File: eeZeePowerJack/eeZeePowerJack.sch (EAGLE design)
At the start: 10 parts, among them J1 POWER_JACKPTH, U2 LD29150DT

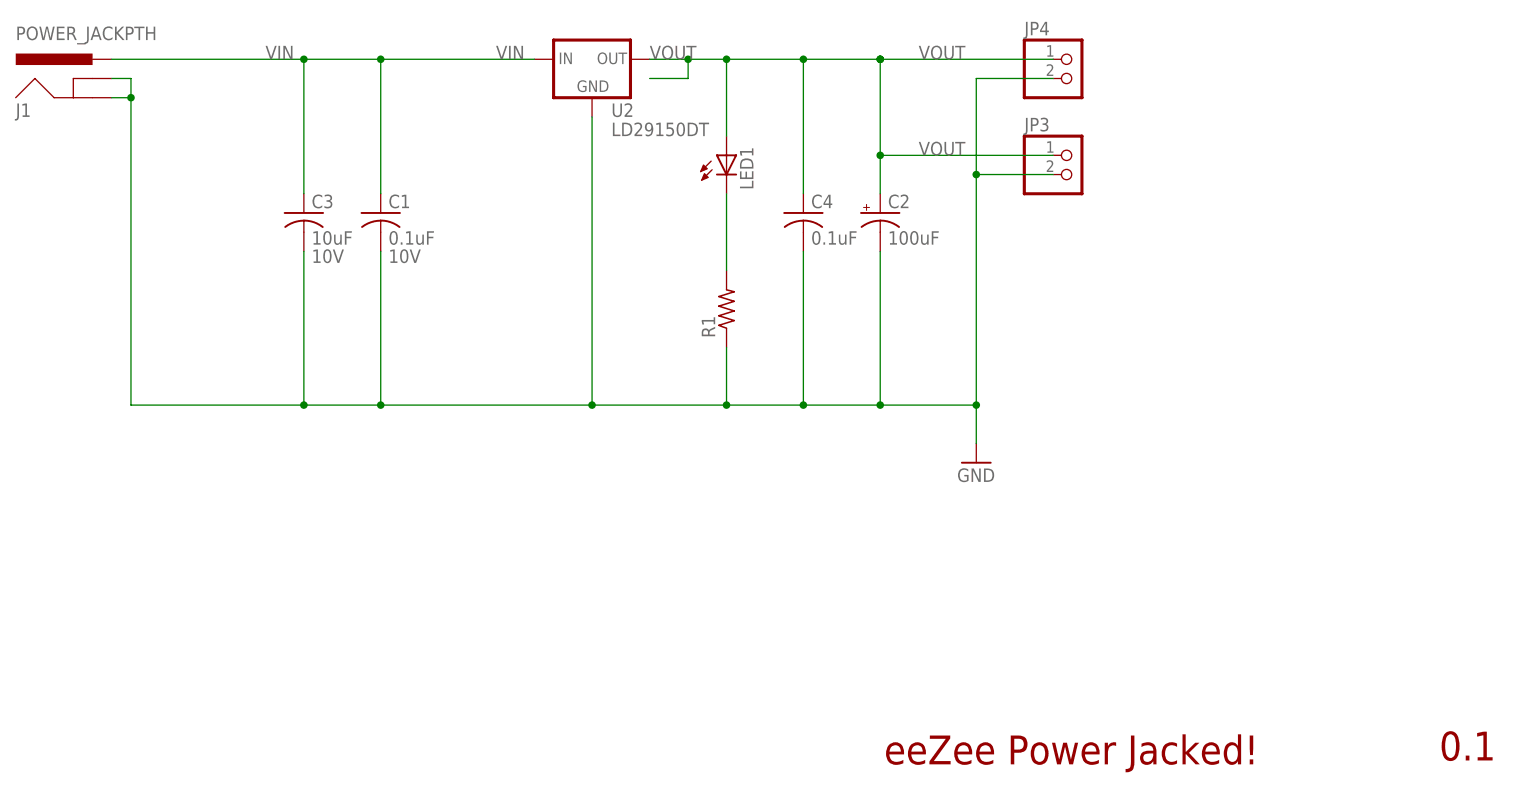
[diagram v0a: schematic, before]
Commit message: Revised to use standard 1206 10uF part, moved bot thoughts silk.
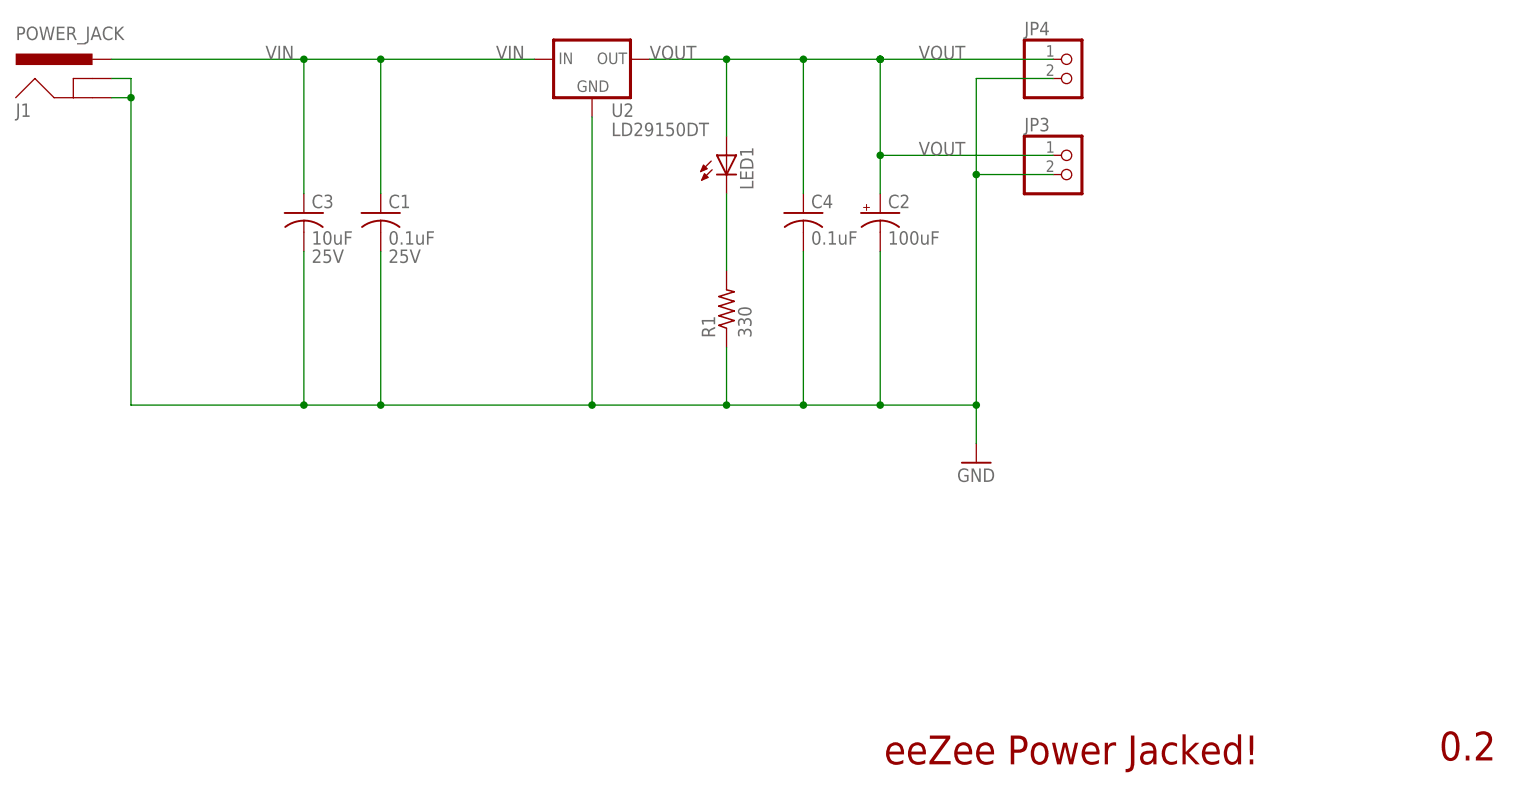
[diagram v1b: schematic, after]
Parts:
- C1: VOLTAGE 10V -> 25V
- C3: device rcl:C-USC0603 -> rcl:C-USC1206; VOLTAGE 10V -> 25V
- J1: value POWER_JACKPTH -> POWER_JACK
- R1: value (none) -> 330
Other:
- note added: "0.2"
- note removed: "0.1"
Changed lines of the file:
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@@
 <part name="LED1" library="led" deviceset="LED" device="CHIPLED_1206"/>
 <part name="C1" library="rcl" deviceset="C-US" device="C0603" value="0.1uF">
-<attribute name="VOLTAGE" value="10V"/>
+<attribute name="VOLTAGE" value="25V"/>
 </part>
 <part name="C2" library="rcl" deviceset="CPOL-US" device="SMCB" value="100uF"/>
-<part name="R1" library="resistor" deviceset="R-US_" device="R0603"/>
-<part name="C3" library="rcl" deviceset="C-US" device="C0603" value="10uF">
-<attribute name="VOLTAGE" value="10V"/>
+<part name="R1" library="resistor" deviceset="R-US_" device="R0603" value="330"/>
+<part name="C3" library="rcl" deviceset="C-US" device="C1206" value="10uF">
+<attribute name="VOLTAGE" value="25V"/>
 </part>
 <part name="FRAME1" library="mes" deviceset="LETTER_L" device=""/>
@@
 <part name="JP3" library="pinhead-2" deviceset="PINHD-1X02" device="_2.54-S"/>
 <part name="JP4" library="pinhead-2" deviceset="PINHD-1X02" device="_2.54-S"/>
-<part name="J1" library="SparkFun-Connectors" deviceset="POWER_JACK" device="PTH"/>
+<part name="J1" library="SparkFun-Connectors" deviceset="POWER_JACK" device="PTH" value="POWER_JACK"/>
 <part name="U2" library="bt_regulator" deviceset="LD29150" device="DT"/>
 </parts>
@@
 <plain>
 <text x="160.528" y="23.622" size="3.81" layer="94">eeZee Power Jacked!</text>
-<text x="233.934" y="24.13" size="3.81" layer="94">0.1</text>
+<text x="233.934" y="24.13" size="3.81" layer="94">0.2</text>
 </plain>
 <instances>
@@
 <net name="VOUT" class="0">
 <segment>
-<wire x1="129.54" y1="114.3" x2="134.62" y2="114.3" width="0.1524" layer="91"/>
-<wire x1="134.62" y1="116.84" x2="129.54" y2="116.84" width="0.1524" layer="91"/>
-<wire x1="134.62" y1="116.84" x2="139.7" y2="116.84" width="0.1524" layer="91"/>
+<wire x1="129.54" y1="116.84" x2="139.7" y2="116.84" width="0.1524" layer="91"/>
 <junction x="160.02" y="116.84"/>
 <pinref part="C2" gate="G$1" pin="+"/>
@@
 <label x="165.1" y="116.84" size="1.778" layer="95"/>
 <junction x="149.86" y="116.84"/>
-<wire x1="134.62" y1="114.3" x2="134.62" y2="116.84" width="0.1524" layer="91"/>
-<junction x="134.62" y="116.84"/>
 <junction x="160.02" y="104.14"/>
 <pinref part="LED1" gate="G$1" pin="A"/>

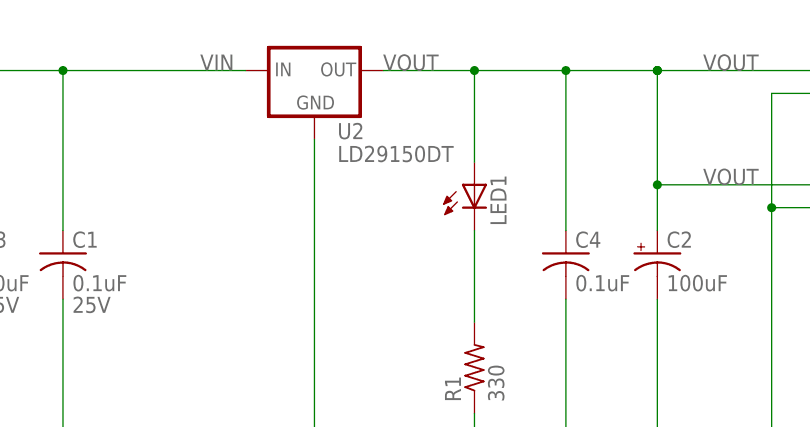
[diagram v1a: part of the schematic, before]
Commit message: Replaced regulator with a lower cost one. Rearranged layout. Regulator on top (heat), capacitors on the bottom. Labeling rearranged.
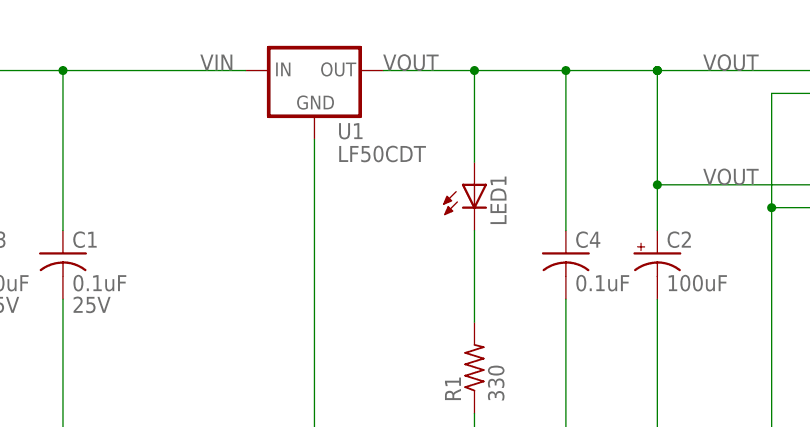
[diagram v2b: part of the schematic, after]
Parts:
- removed U2: LD29150DT, bt_regulator:LD29150DT
- added U1: LF50CDT, bt_regulator:LF50CDT
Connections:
- net GND: now also U1.GND; no longer U2.GND
- net VIN: now also U1.VIN; no longer U2.VIN
- net VOUT: now also U1.VOUT; no longer U2.VOUT
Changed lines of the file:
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@@
 <grid distance="0.1" unitdist="inch" unit="inch" style="lines" multiple="1" display="no" altdistance="0.01" altunitdist="inch" altunit="inch"/>
 <layers>
-<layer number="1" name="Top" color="4" fill="1" visible="yes" active="no"/>
-<layer number="16" name="Bottom" color="1" fill="1" visible="yes" active="no"/>
-<layer number="17" name="Pads" color="2" fill="1" visible="yes" active="no"/>
-<layer number="18" name="Vias" color="2" fill="1" visible="yes" active="no"/>
-<layer number="19" name="Unrouted" color="6" fill="1" visible="yes" active="no"/>
-<layer number="20" name="Dimension" color="15" fill="1" visible="yes" active="no"/>
-<layer number="21" name="tPlace" color="7" fill="1" visible="yes" active="no"/>
-<layer number="22" name="bPlace" color="7" fill="1" visible="yes" active="no"/>
-<layer number="23" name="tOrigins" color="15" fill="1" visible="yes" active="no"/>
-<layer number="24" name="bOrigins" color="15" fill="1" visible="yes" active="no"/>
-<layer number="25" name="tNames" color="7" fill="1" visible="yes" active="no"/>
-<layer number="26" name="bNames" color="7" fill="1" visible="yes" active="no"/>
-<layer number="27" name="tValues" color="7" fill="1" visible="yes" active="no"/>
-<layer number="28" name="bValues" color="7" fill="1" visible="yes" active="no"/>
+<layer number="1" name="Top" color="4" fill="1" visible="no" active="no"/>
+<layer number="16" name="Bottom" color="1" fill="1" visible="no" active="no"/>
+<layer number="17" name="Pads" color="2" fill="1" visible="no" active="no"/>
+<layer number="18" name="Vias" color="2" fill="1" visible="no" active="no"/>
+<layer number="19" name="Unrouted" color="6" fill="1" visible="no" active="no"/>
+<layer number="20" name="Dimension" color="15" fill="1" visible="no" active="no"/>
+<layer number="21" name="tPlace" color="7" fill="1" visible="no" active="no"/>
+<layer number="22" name="bPlace" color="7" fill="1" visible="no" active="no"/>
+<layer number="23" name="tOrigins" color="15" fill="1" visible="no" active="no"/>
+<layer number="24" name="bOrigins" color="15" fill="1" visible="no" active="no"/>
+<layer number="25" name="tNames" color="7" fill="1" visible="no" active="no"/>
+<layer number="26" name="bNames" color="7" fill="1" visible="no" active="no"/>
+<layer number="27" name="tValues" color="7" fill="1" visible="no" active="no"/>
+<layer number="28" name="bValues" color="7" fill="1" visible="no" active="no"/>
 <layer number="29" name="tStop" color="7" fill="3" visible="no" active="no"/>
 <layer number="30" name="bStop" color="7" fill="6" visible="no" active="no"/>
@@
 <layer number="35" name="tGlue" color="7" fill="4" visible="no" active="no"/>
 <layer number="36" name="bGlue" color="7" fill="5" visible="no" active="no"/>
-<layer number="37" name="tTest" color="7" fill="1" visible="yes" active="no"/>
-<layer number="38" name="bTest" color="7" fill="1" visible="yes" active="no"/>
+<layer number="37" name="tTest" color="7" fill="1" visible="no" active="no"/>
+<layer number="38" name="bTest" color="7" fill="1" visible="no" active="no"/>
 <layer number="39" name="tKeepout" color="4" fill="11" visible="no" active="no"/>
 <layer number="40" name="bKeepout" color="1" fill="11" visible="no" active="no"/>
@@
 <layer number="44" name="Drills" color="7" fill="1" visible="no" active="no"/>
 <layer number="45" name="Holes" color="7" fill="1" visible="no" active="no"/>
-<layer number="46" name="Milling" color="3" fill="1" visible="yes" active="no"/>
-<layer number="47" name="Measures" color="7" fill="1" visible="yes" active="no"/>
-<layer number="48" name="Document" color="7" fill="1" visible="yes" active="no"/>
-<layer number="49" name="Reference" color="7" fill="1" visible="yes" active="no"/>
-<layer number="50" name="dxf" color="7" fill="1" visible="yes" active="no"/>
-<layer number="51" name="tDocu" color="7" fill="1" visible="yes" active="no"/>
-<layer number="52" name="bDocu" color="7" fill="1" visible="yes" active="no"/>
-<layer number="53" name="tGND_GNDA" color="7" fill="9" visible="yes" active="no"/>
-<layer number="54" name="bGND_GNDA" color="1" fill="9" visible="yes" active="no"/>
-<layer number="56" name="wert" color="7" fill="1" visible="yes" active="no"/>
+<layer number="46" name="Milling" color="3" fill="1" visible="no" active="no"/>
+<layer number="47" name="Measures" color="7" fill="1" visible="no" active="no"/>
+<layer number="48" name="Document" color="7" fill="1" visible="no" active="no"/>
+<layer number="49" name="Reference" color="7" fill="1" visible="no" active="no"/>
+<layer number="50" name="dxf" color="7" fill="1" visible="no" active="no"/>
+<layer number="51" name="tDocu" color="7" fill="1" visible="no" active="no"/>
+<layer number="52" name="bDocu" color="7" fill="1" visible="no" active="no"/>
+<layer number="53" name="tGND_GNDA" color="7" fill="9" visible="no" active="no"/>
+<layer number="54" name="bGND_GNDA" color="1" fill="9" visible="no" active="no"/>
+<layer number="56" name="wert" color="7" fill="1" visible="no" active="no"/>
 <layer number="91" name="Nets" color="2" fill="1" visible="yes" active="yes"/>
 <layer number="92" name="Busses" color="1" fill="1" visible="yes" active="yes"/>
@@
 <part name="JP4" library="pinhead-2" deviceset="PINHD-1X02" device="_2.54-S"/>
 <part name="J1" library="SparkFun-Connectors" deviceset="POWER_JACK" device="PTH" value="POWER_JACK"/>
-<part name="U2" library="bt_regulator" deviceset="LD29150" device="DT"/>
+<part name="U1" library="bt_regulator" deviceset="LF50CDT" device=""/>
 </parts>
 <sheets>
@@
 <instance part="JP4" gate="A" x="185.42" y="114.3"/>
 <instance part="J1" gate="G$1" x="55.88" y="109.22"/>
-<instance part="U2" gate="G$1" x="121.92" y="114.3"/>
+<instance part="U1" gate="LF50CDT" x="121.92" y="114.3"/>
 </instances>
 <busses>
@@
 <junction x="83.82" y="116.84"/>
 <label x="109.22" y="116.84" size="1.778" layer="95"/>
-<pinref part="U2" gate="G$1" pin="VIN"/>
+<pinref part="U1" gate="LF50CDT" pin="VIN"/>
 </segment>
 <segment>
@@
 <wire x1="139.7" y1="78.74" x2="139.7" y2="71.12" width="0.1524" layer="91"/>
 <junction x="139.7" y="71.12"/>
-<pinref part="U2" gate="G$1" pin="GND"/>
+<pinref part="U1" gate="LF50CDT" pin="GND"/>
 </segment>
 </net>
@@
 <wire x1="139.7" y1="106.68" x2="139.7" y2="116.84" width="0.1524" layer="91"/>
 <junction x="139.7" y="116.84"/>
-<pinref part="U2" gate="G$1" pin="VOUT"/>
-</segment>
-</net>
+<pinref part="U1" gate="LF50CDT" pin="VOUT"/>
+</segment>
+</net>
